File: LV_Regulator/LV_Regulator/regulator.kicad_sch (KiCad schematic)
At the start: 55 parts, among them U4 BQ25858QWRRVRQ1, U5 CSD19506KTT, U6 CSD19506KTT, U7 CSD19506KTT, U8 CSD19506KTT

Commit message: Fixed DRC & some other minor tweaks
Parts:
- C28, C29: Purchase place https://eu.mouser.com/ProductDetail/KEMET/C1206C104K1RAC786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 -> (none)
- C31: Buying Place https://eu.mouser.com/ProductDetail/Nichicon/UPM1J560MPD1TD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 -> (none); Purchase Place (none) -> https://eu.mouser.com/ProductDetail/Nichicon/UPM1J560MPD1TD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
- C34: Buying Place https://eu.mouser.com/ProductDetail/Nichicon/UCZ1J181MNS1MS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 -> (none); Purchase Place (none) -> https://eu.mouser.com/ProductDetail/Nichicon/UCZ1J181MNS1MS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
- R28: Purchase Place (none) -> https://eu.mouser.com/ProductDetail/KOA-Speer/RN73H2BTTD132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; purchase place https://eu.mouser.com/ProductDetail/KOA-Speer/RN73H2BTTD132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 -> (none)
- R51, R52: Purchase Place (none) -> https://eu.mouser.com/ProductDetail/TDK/CGA5L1C0G2A104J160A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
- R54: Purchase place https://eu.mouser.com/ProductDetail/Panasonic/ERJ-T08J103V?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 -> (none)
- U4: Purchase Place (none) -> https://eu.mouser.com/ProductDetail/Texas-Instruments/BQ258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
- U5, U6, U7, U8: Purchase Place (none) -> https://eu.mouser.com/ProductDetail/Texas-Instruments/CSD19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

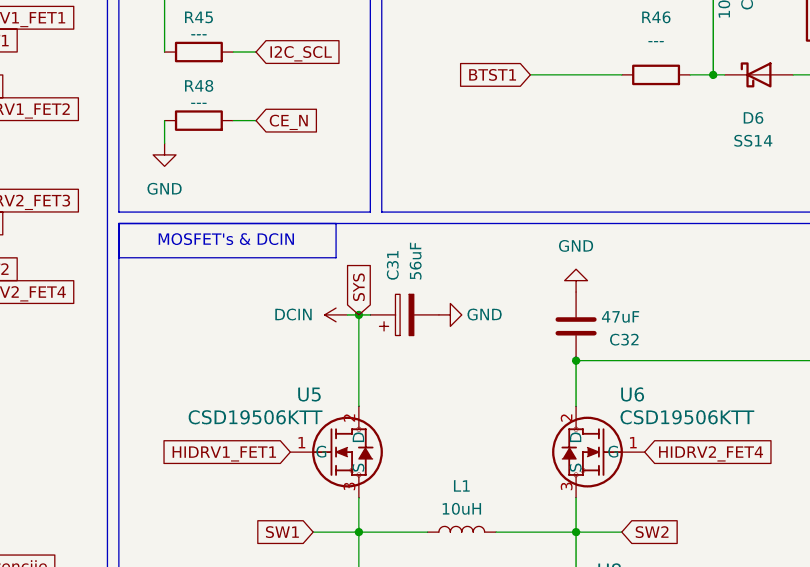
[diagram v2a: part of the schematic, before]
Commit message: Finished BoM Sheet, Fixed Component issues.
Fixed DRC Errors, as well as changing a Capacitor that was not chosen correctly. And have filled Bill of Materials.
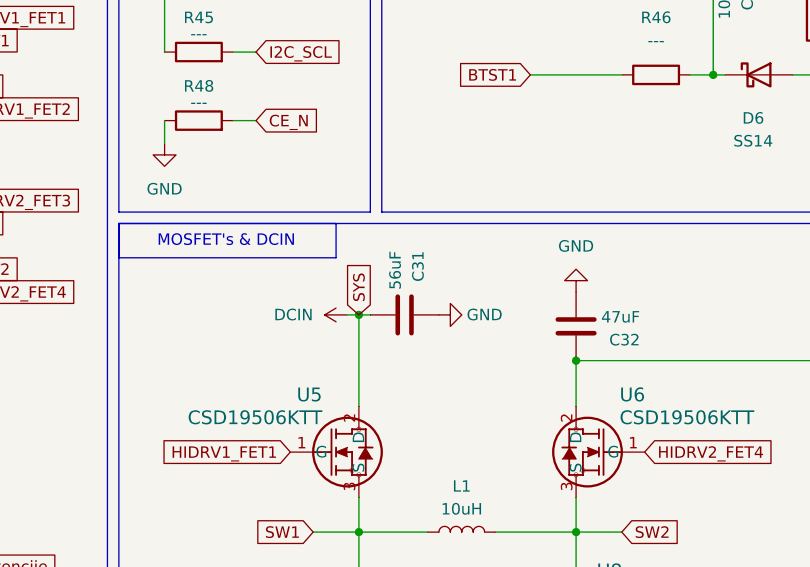
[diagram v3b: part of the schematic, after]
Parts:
- removed C31: 56uF, ul_UCZ1J181MNQ1MS:CAP_UCD_12P5X13P5_NCH, symbol Device:C_Polarized
- added C31: 56uF, Capacitor_SMD:C_1206_3216Metric_Pad1.33x1.80mm_HandSolder, symbol Device:C
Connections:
- net DCIN: now also C31.2
- net GND: now also C31.1
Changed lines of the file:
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@@
 	)
 	(symbol
+		(lib_id "Device:C")
+		(at 166.37 104.14 270)
+		(unit 1)
+		(body_style 1)
+		(exclude_from_sim no)
+		(in_bom yes)
+		(on_board yes)
+		(in_pos_files yes)
+		(dnp no)
+		(property "Reference" "C31"
+			(at 167.894 97.028 0)
+			(show_name no)
+			(do_not_autoplace no)
+			(effects
+				(font
+					(size 1.27 1.27)
+				)
+				(justify left)
+			)
+		)
+		(property "Value" "56uF"
+			(at 165.354 97.028 0)
+			(show_name no)
+			(do_not_autoplace no)
+			(effects
+				(font
+					(size 1.27 1.27)
+				)
+				(justify left)
+			)
+		)
+		(property "Footprint" "Capacitor_SMD:C_1206_3216Metric_Pad1.33x1.80mm_HandSolder"
+			(at 162.56 105.1052 0)
+			(hide yes)
+			(show_name no)
+			(do_not_autoplace no)
+			(effects
+				(font
+					(size 1.27 1.27)
+				)
+			)
+		)
+		(property "Datasheet" ""
+			(at 166.37 104.14 0)
+			(hide yes)
+			(show_name no)
+			(do_not_autoplace no)
+			(effects
+				(font
+					(size 1.27 1.27)
+				)
+			)
+		)
+		(property "Description" "Unpolarized capacitor"
+			(at 166.37 104.14 0)
+			(hide yes)
+			(show_name no)
+			(do_not_autoplace no)
+			(effects
+				(font
+					(size 1.27 1.27)
+				)
+			)
+		)
+		(property "Purchase Place" "https://eu.mouser.com/ProductDetail/YAGEO/CC1206JRNPO0BN560?qs=AgBp2OyFlx%252BW%2FnaeCGBiHg%3D%3D"
+			(at 166.37 104.14 0)
+			(hide yes)
+			(show_name no)
+			(do_not_autoplace no)
+			(effects
+				(font
+					(size 1.27 1.27)
+				)
+			)
+		)
+		(property "Buying Place" ""
+			(at 166.37 104.14 0)
+			(hide yes)
+			(show_name no)
+			(do_not_autoplace no)
+			(effects
+				(font
+					(size 1.27 1.27)
+				)
+			)
+		)
+		(property "MPN" ""
+			(at 166.37 104.14 0)
+			(hide yes)
+			(show_name no)
+			(do_not_autoplace no)
+			(effects
+				(font
+					(size 1.27 1.27)
+				)
+			)
+		)
+		(property "OC_FARNELL" ""
+			(at 166.37 104.14 0)
+			(hide yes)
+			(show_name no)
+			(do_not_autoplace no)
+			(effects
+				(font
+					(size 1.27 1.27)
+				)
+			)
+		)
+		(property "OC_NEWARK" ""
+			(at 166.37 104.14 0)
+			(hide yes)
+			(show_name no)
+			(do_not_autoplace no)
+			(effects
+				(font
+					(size 1.27 1.27)
+				)
+			)
+		)
+		(property "SUPPLIER" ""
+			(at 166.37 104.14 0)
+			(hide yes)
+			(show_name no)
+			(do_not_autoplace no)
+			(effects
+				(font
+					(size 1.27 1.27)
+				)
+			)
+		)
+		(pin "1"
+		)
+		(pin "2"
+		)
+		(instances
+			(project "LV_Regulator"
+				(path "/9003ce10-3354-47c9-924a-fd038a206791/7dfce8f1-0c22-480c-91d4-3ffb0e2b2dff"
+					(reference "C31")
+					(unit 1)
+				)
+			)
+		)
+	)
+	(symbol
 		(lib_id "power:GND")
 		(at 161.29 144.78 0)
@@
 					(unit 1)
 				)
-			)
-		)
-	)
-	(symbol
-		(lib_id "Device:C_Polarized")
-		(at 166.37 104.14 90)
-		(unit 1)
-		(body_style 1)
-		(exclude_from_sim no)
-		(in_bom yes)
-		(on_board yes)
-		(in_pos_files yes)
-		(dnp no)
-		(property "Reference" "C31"
-			(at 165.1 100.33 0)
-			(show_name no)
-			(do_not_autoplace no)
-			(effects
-				(font
-					(size 1.27 1.27)
-				)
-				(justify left)
-			)
-		)
-		(property "Value" "56uF"
-			(at 167.64 100.33 0)
-			(show_name no)
-			(do_not_autoplace no)
-			(effects
-				(font
-					(size 1.27 1.27)
-				)
-				(justify left)
-			)
-		)
-		(property "Footprint" "ul_UCZ1J181MNQ1MS:CAP_UCD_12P5X13P5_NCH"
-			(at 170.18 103.1748 0)
-			(hide yes)
-			(show_name no)
-			(do_not_autoplace no)
-			(effects
-				(font
-					(size 1.27 1.27)
-				)
-			)
-		)
-		(property "Datasheet" ""
-			(at 166.37 104.14 0)
-			(hide yes)
-			(show_name no)
-			(do_not_autoplace no)
-			(effects
-				(font
-					(size 1.27 1.27)
-				)
-			)
-		)
-		(property "Description" "Polarized capacitor"
-			(at 166.37 104.14 0)
-			(hide yes)
-			(show_name no)
-			(do_not_autoplace no)
-			(effects
-				(font
-					(size 1.27 1.27)
-				)
-			)
-		)
-		(property "Purchase Place" "https://eu.mouser.com/ProductDetail/Nichicon/UPM1J560MPD1TD?qs=sGAEpiMZZMsh%252B1woXyUXjxqqPit2tXVBZePDpSS4NTc%3D"
-			(at 166.37 104.14 0)
-			(hide yes)
-			(show_name no)
-			(do_not_autoplace no)
-			(effects
-				(font
-					(size 1.27 1.27)
-				)
-			)
-		)
-		(property "Buying Place" ""
-			(at 166.37 104.14 0)
-			(hide yes)
-			(show_name no)
-			(do_not_autoplace no)
-			(effects
-				(font
-					(size 1.27 1.27)
-				)
-			)
-		)
-		(property "MPN" ""
-			(at 166.37 104.14 0)
-			(hide yes)
-			(show_name no)
-			(do_not_autoplace no)
-			(effects
-				(font
-					(size 1.27 1.27)
-				)
-			)
-		)
-		(property "OC_FARNELL" ""
-			(at 166.37 104.14 0)
-			(hide yes)
-			(show_name no)
-			(do_not_autoplace no)
-			(effects
-				(font
-					(size 1.27 1.27)
-				)
-			)
-		)
-		(property "OC_NEWARK" ""
-			(at 166.37 104.14 0)
-			(hide yes)
-			(show_name no)
-			(do_not_autoplace no)
-			(effects
-				(font
-					(size 1.27 1.27)
-				)
-			)
-		)
-		(property "SUPPLIER" ""
-			(at 166.37 104.14 0)
-			(hide yes)
-			(show_name no)
-			(do_not_autoplace no)
-			(effects
-				(font
-					(size 1.27 1.27)
-				)
-			)
-		)
-		(pin "1"
-		)
-		(pin "2"
-		)
-		(instances
-			(project "LV_Regulator"
-				(path "/9003ce10-3354-47c9-924a-fd038a206791/7dfce8f1-0c22-480c-91d4-3ffb0e2b2dff"
-					(reference "C31")
-					(unit 1)
-				)

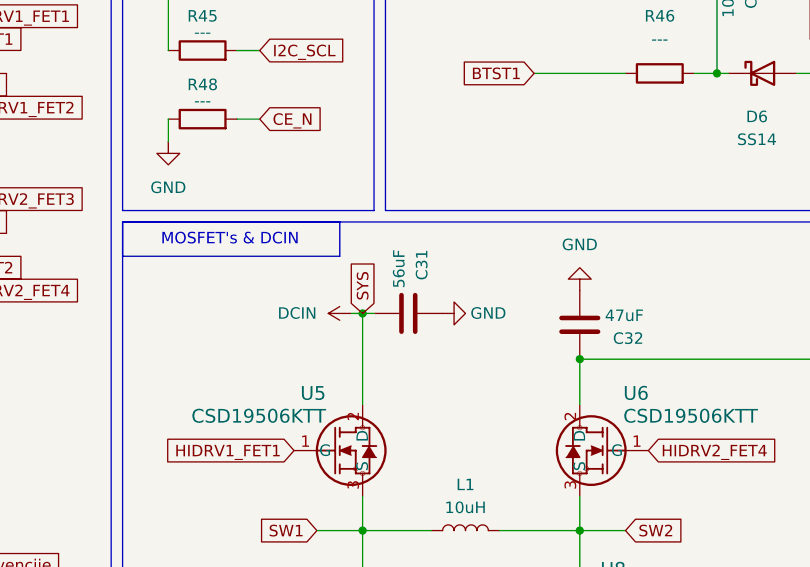
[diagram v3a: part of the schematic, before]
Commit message: Fixed Capacitor choice
Mixed up Capacitor choices, fixed the issue
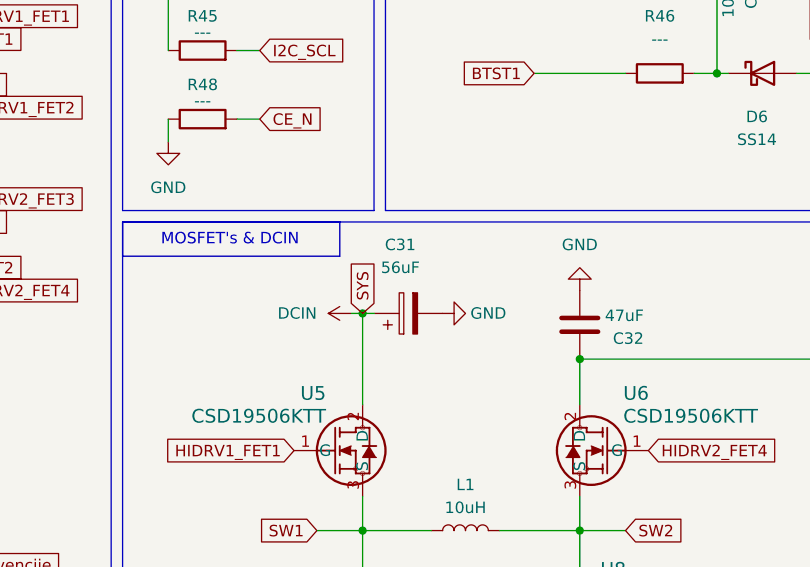
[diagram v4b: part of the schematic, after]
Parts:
- removed C31: 56uF, Capacitor_SMD:C_1206_3216Metric_Pad1.33x1.80mm_HandSolder, symbol Device:C
- added C31: 56uF, Capacitor_SMD:CP_Elec_10x10, symbol Device:C_Polarized
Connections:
- net DCIN: now also C31.1
- net GND: now also C31.2
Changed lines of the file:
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@@
+	)
+	(symbol
+		(lib_id "Device:C_Polarized")
+		(at 166.37 104.14 90)
+		(unit 1)
+		(body_style 1)
+		(exclude_from_sim no)
+		(in_bom yes)
+		(on_board yes)
+		(in_pos_files yes)
+		(dnp no)
+		(fields_autoplaced yes)
+		(property "Reference" "C31"
+			(at 165.481 96.52 90)
+			(show_name no)
+			(do_not_autoplace no)
+			(effects
+				(font
+					(size 1.27 1.27)
+				)
+			)
+		)
+		(property "Value" "56uF"
+			(at 165.481 99.06 90)
+			(show_name no)
+			(do_not_autoplace no)
+			(effects
+				(font
+					(size 1.27 1.27)
+				)
+			)
+		)
+		(property "Footprint" "Capacitor_SMD:CP_Elec_10x10"
+			(at 170.18 103.1748 0)
+			(hide yes)
+			(show_name no)
+			(do_not_autoplace no)
+			(effects
+				(font
+					(size 1.27 1.27)
+				)
+			)
+		)
+		(property "Datasheet" "https://www.eaton.com/content/dam/eaton/products/electronic-components/resources/data-sheet/eaton-ehbsa-hybrid-aluminum-electrolytic-capacitor-data-sheet-elx1481-en.pdf"
+			(at 166.37 104.14 0)
+			(hide yes)
+			(show_name no)
+			(do_not_autoplace no)
+			(effects
+				(font
+					(size 1.27 1.27)
+				)
+			)
+		)
+		(property "Description" "Polarized capacitor"
+			(at 166.37 104.14 0)
+			(hide yes)
+			(show_name no)
+			(do_not_autoplace no)
+			(effects
+				(font
+					(size 1.27 1.27)
+				)
+			)
+		)
+		(property "Purchase Place" "https://eu.mouser.com/ProductDetail/Eaton-Electronics/EHBSA080M5601010T?qs=sGAEpiMZZMsh%252B1woXyUXjyUUqvU%2FlejKTQ9mdTwBEYY%3D"
+			(at 166.37 104.14 90)
+			(hide yes)
+			(show_name no)
+			(do_not_autoplace no)
+			(effects
+				(font
+					(size 1.27 1.27)
+				)
+			)
+		)
+		(pin "2"
+		)
+		(pin "1"
+		)
+		(instances
+			(project "LV_Regulator"
+				(path "/9003ce10-3354-47c9-924a-fd038a206791/7dfce8f1-0c22-480c-91d4-3ffb0e2b2dff"
+					(reference "C31")
+					(unit 1)
+				)
+			)
+		)
 	)
 	(symbol
@@
 					(unit 1)
 				)
-			)
-		)
-	)
-	(symbol
-		(lib_id "Device:C")
-		(at 166.37 104.14 270)
-		(unit 1)
-		(body_style 1)
-		(exclude_from_sim no)
-		(in_bom yes)
-		(on_board yes)
-		(in_pos_files yes)
-		(dnp no)
-		(property "Reference" "C31"
-			(at 167.894 97.028 0)
-			(show_name no)
-			(do_not_autoplace no)
-			(effects
-				(font
-					(size 1.27 1.27)
-				)
-				(justify left)
-			)
-		)
-		(property "Value" "56uF"
-			(at 165.354 97.028 0)
-			(show_name no)
-			(do_not_autoplace no)
-			(effects
-				(font
-					(size 1.27 1.27)
-				)
-				(justify left)
-			)
-		)
-		(property "Footprint" "Capacitor_SMD:C_1206_3216Metric_Pad1.33x1.80mm_HandSolder"
-			(at 162.56 105.1052 0)
-			(hide yes)
-			(show_name no)
-			(do_not_autoplace no)
-			(effects
-				(font
-					(size 1.27 1.27)
-				)
-			)
-		)
-		(property "Datasheet" ""
-			(at 166.37 104.14 0)
-			(hide yes)
-			(show_name no)
-			(do_not_autoplace no)
-			(effects
-				(font
-					(size 1.27 1.27)
-				)
-			)
-		)
-		(property "Description" "Unpolarized capacitor"
-			(at 166.37 104.14 0)
-			(hide yes)
-			(show_name no)
-			(do_not_autoplace no)
-			(effects
-				(font
-					(size 1.27 1.27)
-				)
-			)
-		)
-		(property "Purchase Place" "https://eu.mouser.com/ProductDetail/YAGEO/CC1206JRNPO0BN560?qs=AgBp2OyFlx%252BW%2FnaeCGBiHg%3D%3D"
-			(at 166.37 104.14 0)
-			(hide yes)
-			(show_name no)
-			(do_not_autoplace no)
-			(effects
-				(font
-					(size 1.27 1.27)
-				)
-			)
-		)
-		(property "Buying Place" ""
-			(at 166.37 104.14 0)
-			(hide yes)
-			(show_name no)
-			(do_not_autoplace no)
-			(effects
-				(font
-					(size 1.27 1.27)
-				)
-			)
-		)
-		(property "MPN" ""
-			(at 166.37 104.14 0)
-			(hide yes)
-			(show_name no)
-			(do_not_autoplace no)
-			(effects
-				(font
-					(size 1.27 1.27)
-				)
-			)
-		)
-		(property "OC_FARNELL" ""
-			(at 166.37 104.14 0)
-			(hide yes)
-			(show_name no)
-			(do_not_autoplace no)
-			(effects
-				(font
-					(size 1.27 1.27)
-				)
-			)
-		)
-		(property "OC_NEWARK" ""
-			(at 166.37 104.14 0)
-			(hide yes)
-			(show_name no)
-			(do_not_autoplace no)
-			(effects
-				(font
-					(size 1.27 1.27)
-				)
-			)
-		)
-		(property "SUPPLIER" ""
-			(at 166.37 104.14 0)
-			(hide yes)
-			(show_name no)
-			(do_not_autoplace no)
-			(effects
-				(font
-					(size 1.27 1.27)
-				)
-			)
-		)
-		(pin "1"
-		)
-		(pin "2"
-		)
-		(instances
-			(project "LV_Regulator"
-				(path "/9003ce10-3354-47c9-924a-fd038a206791/7dfce8f1-0c22-480c-91d4-3ffb0e2b2dff"
-					(reference "C31")
-					(unit 1)
-				)
